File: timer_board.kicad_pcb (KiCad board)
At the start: 2 copper layers, 127 x 76.2 mm, 53 parts, among them IC1 ATMEGA32U4, K1 T9AS5D22-5, P1 USBMICRO, P2 OUT_INV, P3 Trigger, P4 OUT, Q1 NPN, Q2 NPN, U1 DS3231N, U2 74HC04, Y1 RESONATORSMD

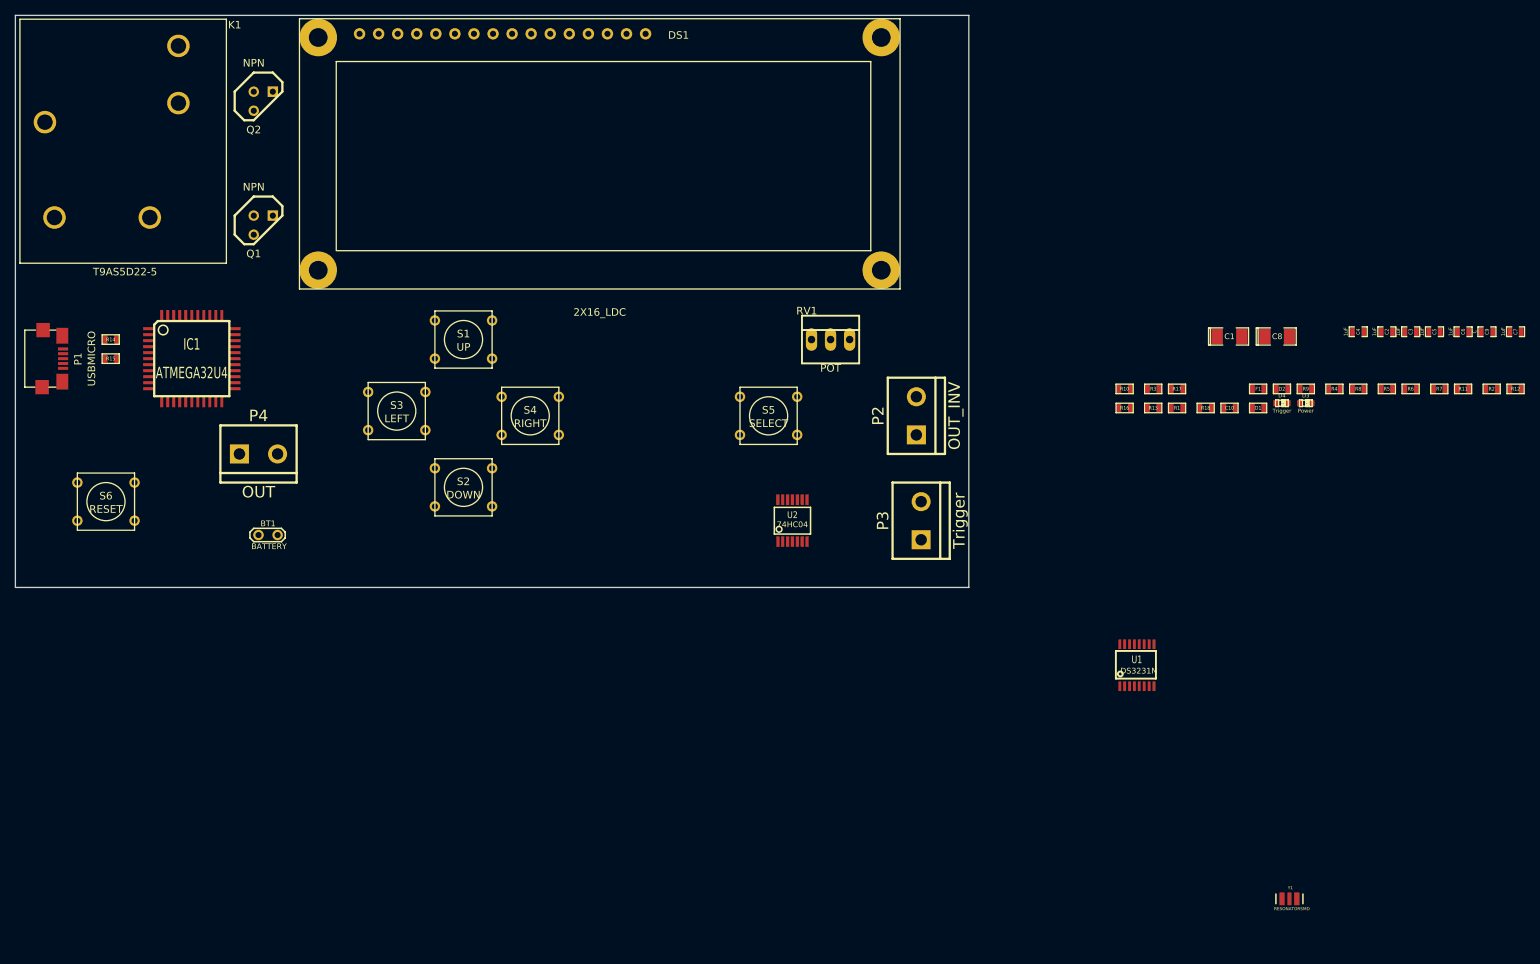
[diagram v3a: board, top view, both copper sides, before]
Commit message: Added battery holder
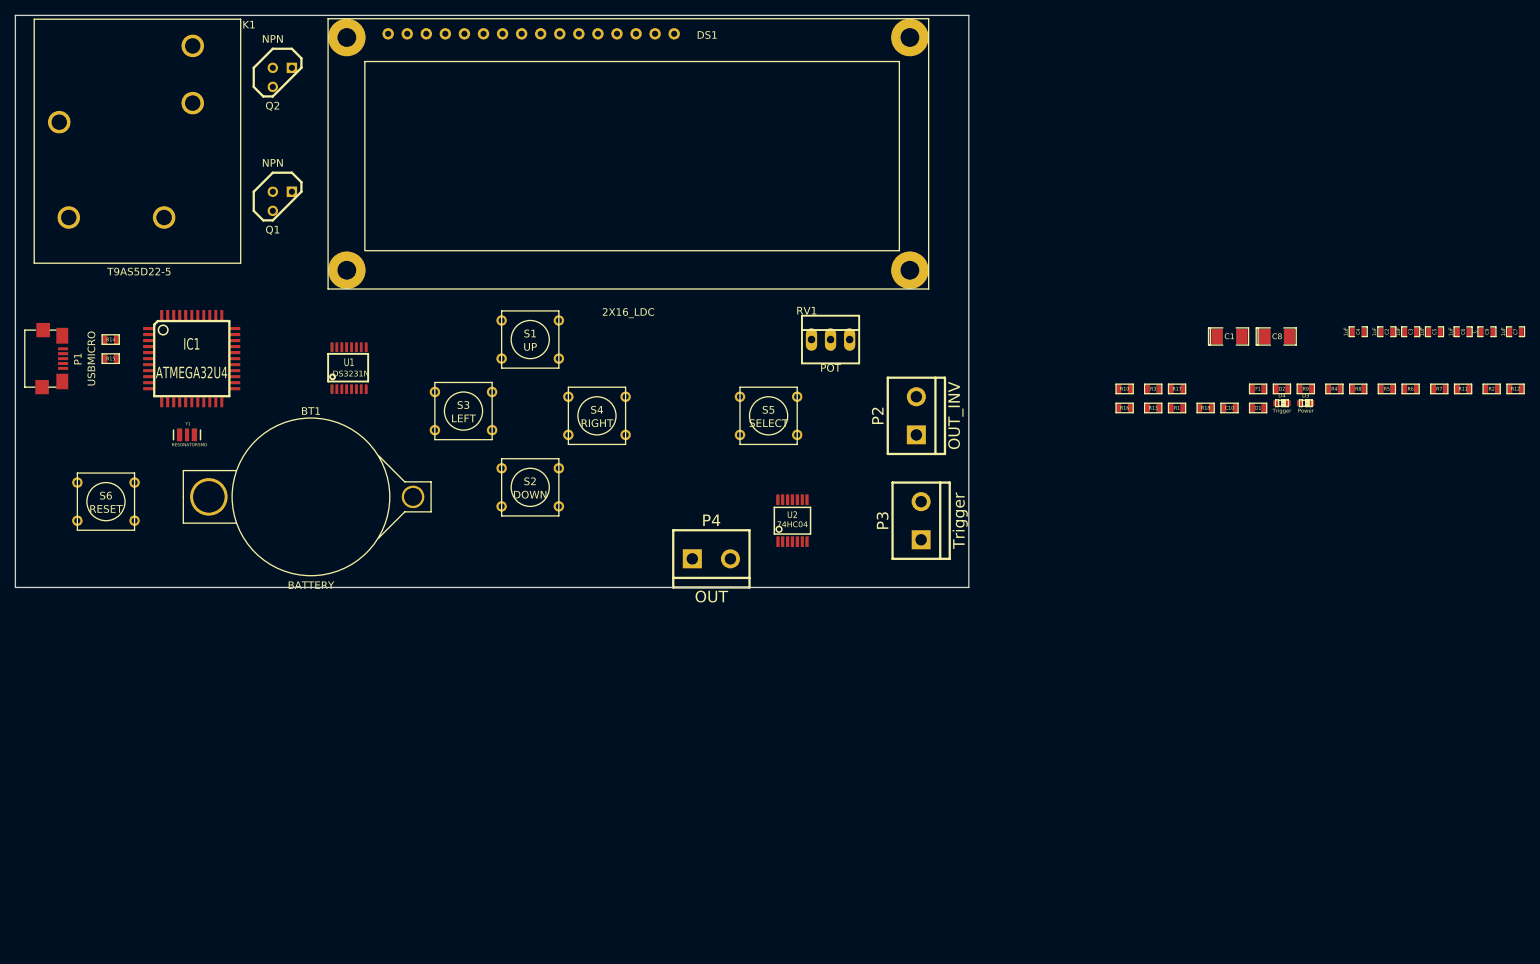
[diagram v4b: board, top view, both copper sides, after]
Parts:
- BT1: footprint TESTPOINT -> CR2032
- moved Y1 159.3 mm to (48.3, 81.3)
- moved U1 112.1 mm to (69.8, 72.4)
- moved P4 61.9 mm to (118.1, 97.8)
- moved S1 8.89 mm to (94.0, 68.6)
- moved S2 8.89 mm to (94.0, 88.3)
- moved S3 8.89 mm to (85.1, 78.1)
- moved S4 8.89 mm to (102.9, 78.7)
- moved BT1 7.65 mm to (64.8, 89.5)
- moved Q1 4.07 mm to (61.0, 50.2)
- moved Q2 4.07 mm to (61.0, 33.7)
- moved DS1 3.81 mm to (82.5, 29.8)
- moved K1 1.90 mm to (41.9, 41.9)
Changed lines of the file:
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@@
     (mod_text_width 0.15)
     (pad_size 3 3)
-    (pad_drill 2.06)
+    (pad_drill 2.4)
     (pad_to_mask_clearance 0)
     (aux_axis_origin 0 0)
@@
   )
   (module TSSOP16 (layer F.Cu)
-    (at 174.785 111.965)
+    (at 69.85 72.39)
     (attr smd)
     (fp_text reference U1 (at 0 -0.7493) (layer F.SilkS)
@@
   )
   (module TO92 (layer F.Cu)
-    (at 58.42 36.83)
+    (at 60.96 33.655)
     (descr "Transistor TO92 brochage type BC237")
     (tags "TR TO92")
@@
   )
   (module TO92 (layer F.Cu)
-    (at 58.42 53.34)
+    (at 60.96 50.165)
     (descr "Transistor TO92 brochage type BC237")
     (tags "TR TO92")
@@
     )
   )
-  (module TESTPOINT (layer F.Cu)
-    (at 59.055 94.615)
-    (descr "Connecteurs 2 pins")
-    (tags "CONN DEV")
-    (fp_text reference BT1 (at 0 -1.524) (layer F.SilkS)
-      (effects (font (size 0.762 0.762) (thickness 0.1524)))
-    )
-    (fp_text value BATTERY (at 0.127 1.524) (layer F.SilkS)
-      (effects (font (size 0.762 0.762) (thickness 0.1524)))
-    )
-    (fp_line (start -1.905 -0.889) (end 1.778 -0.889) (layer F.SilkS) (width 0.2032))
-    (fp_line (start 1.778 -0.889) (end 2.286 -0.381) (layer F.SilkS) (width 0.2032))
-    (fp_line (start 2.286 -0.381) (end 2.286 0.381) (layer F.SilkS) (width 0.2032))
-    (fp_line (start 2.286 0.381) (end 1.778 0.889) (layer F.SilkS) (width 0.2032))
-    (fp_line (start 1.778 0.889) (end -1.905 0.889) (layer F.SilkS) (width 0.2032))
-    (fp_line (start -1.905 0.889) (end -2.413 0.381) (layer F.SilkS) (width 0.2032))
-    (fp_line (start -2.413 0.381) (end -2.413 -0.381) (layer F.SilkS) (width 0.2032))
-    (fp_line (start -2.413 -0.381) (end -1.905 -0.889) (layer F.SilkS) (width 0.2032))
-    (pad 1 thru_hole circle (at -1.27 0) (size 1.397 1.397) (drill 0.8128)
-      (layers *.Cu *.Mask F.SilkS)
-      (net 31 N-000044)
-    )
-    (pad 1 thru_hole circle (at 1.27 0) (size 1.397 1.397) (drill 0.8128)
-      (layers *.Cu *.Mask F.SilkS)
-      (net 31 N-000044)
-    )
-    (model connectors/testpoint.wrl
-      (at (xyz 0 0 0))
-      (scale (xyz 1 1 1))
-      (rotate (xyz 0 0 0))
-    )
-  )
   (module SW_PUSH_SMALL (layer F.Cu)
     (at 37.465 90.17)
@@
   )
   (module SW_PUSH_SMALL (layer F.Cu)
-    (at 85.09 68.58)
+    (at 93.98 68.58)
     (fp_text reference S1 (at 0 -0.762) (layer F.SilkS)
       (effects (font (size 1.016 1.016) (thickness 0.2032)))
@@
   )
   (module SW_PUSH_SMALL (layer F.Cu)
-    (at 85.09 88.265)
+    (at 93.98 88.265)
     (fp_text reference S2 (at 0 -0.762) (layer F.SilkS)
       (effects (font (size 1.016 1.016) (thickness 0.2032)))
@@
   )
   (module SW_PUSH_SMALL (layer F.Cu)
-    (at 93.98 78.74)
+    (at 102.87 78.74)
     (fp_text reference S4 (at 0 -0.762) (layer F.SilkS)
       (effects (font (size 1.016 1.016) (thickness 0.2032)))
@@
   )
   (module SW_PUSH_SMALL (layer F.Cu)
-    (at 76.2 78.105)
+    (at 85.09 78.105)
     (fp_text reference S3 (at 0 -0.762) (layer F.SilkS)
       (effects (font (size 1.016 1.016) (thickness 0.2032)))
@@
   )
   (module bornier2 (layer F.Cu)
-    (at 57.785 83.82)
+    (at 118.11 97.79)
     (descr "Bornier d'alimentation 2 pins")
     (tags DEV)
@@
   )
   (module LCD16X2 (layer F.Cu)
-    (at 78.74 29.845)
+    (at 82.55 29.845)
     (fp_text reference DS1 (at 35 -1.8) (layer F.SilkS)
       (effects (font (size 1 1) (thickness 0.15)))
@@
   )
   (module T9AS5D22-5 (layer F.Cu)
-    (at 40.005 41.91)
+    (at 41.91 41.91)
     (fp_text reference K1 (at 14.605 -15.24) (layer F.SilkS)
       (effects (font (size 1 1) (thickness 0.15)))
@@
   )
   (module RESONATOR-SMD (layer F.Cu)
-    (at 195.105 143.08)
+    (at 48.26 81.28)
     (attr smd)
     (fp_text reference Y1 (at 0.127 -1.4732) (layer F.SilkS)
@@
     )
   )
+  (module CR2032 (layer F.Cu)
+    (at 64.77 89.535)
+    (fp_text reference BT1 (at 0 -11.4) (layer F.SilkS)
+      (effects (font (size 1 1) (thickness 0.15)))
+    )
+    (fp_text value BATTERY (at 0 11.8) (layer F.SilkS)
+      (effects (font (size 1 1) (thickness 0.15)))
+    )
+    (fp_line (start 12.5 2) (end 9 5.5) (layer F.SilkS) (width 0.15))
+    (fp_line (start 12.5 -2) (end 16 -2) (layer F.SilkS) (width 0.15))
+    (fp_line (start 16 -2) (end 16 2) (layer F.SilkS) (width 0.15))
+    (fp_line (start 16 2) (end 12.5 2) (layer F.SilkS) (width 0.15))
+    (fp_line (start 12.5 -2) (end 9 -5.5) (layer F.SilkS) (width 0.15))
+    (fp_line (start -17 0) (end -17 3.5) (layer F.SilkS) (width 0.15))
+    (fp_line (start -17 3.5) (end -10 3.5) (layer F.SilkS) (width 0.15))
+    (fp_line (start -17 0) (end -17 -3.5) (layer F.SilkS) (width 0.15))
+    (fp_line (start -17 -3.5) (end -10 -3.5) (layer F.SilkS) (width 0.15))
+    (fp_circle (center 0 0) (end 0.1 -10.5) (layer F.SilkS) (width 0.15))
+    (pad 1 thru_hole circle (at -13.6 0) (size 5 5) (drill 4.2)
+      (layers *.Cu *.Mask F.SilkS)
+      (net 31 N-000044)
+    )
+    (pad 2 thru_hole circle (at 13.6 0) (size 3 3) (drill 2.4)
+      (layers *.Cu *.Mask F.SilkS)
+      (net 9 GND)
+    )
+  )

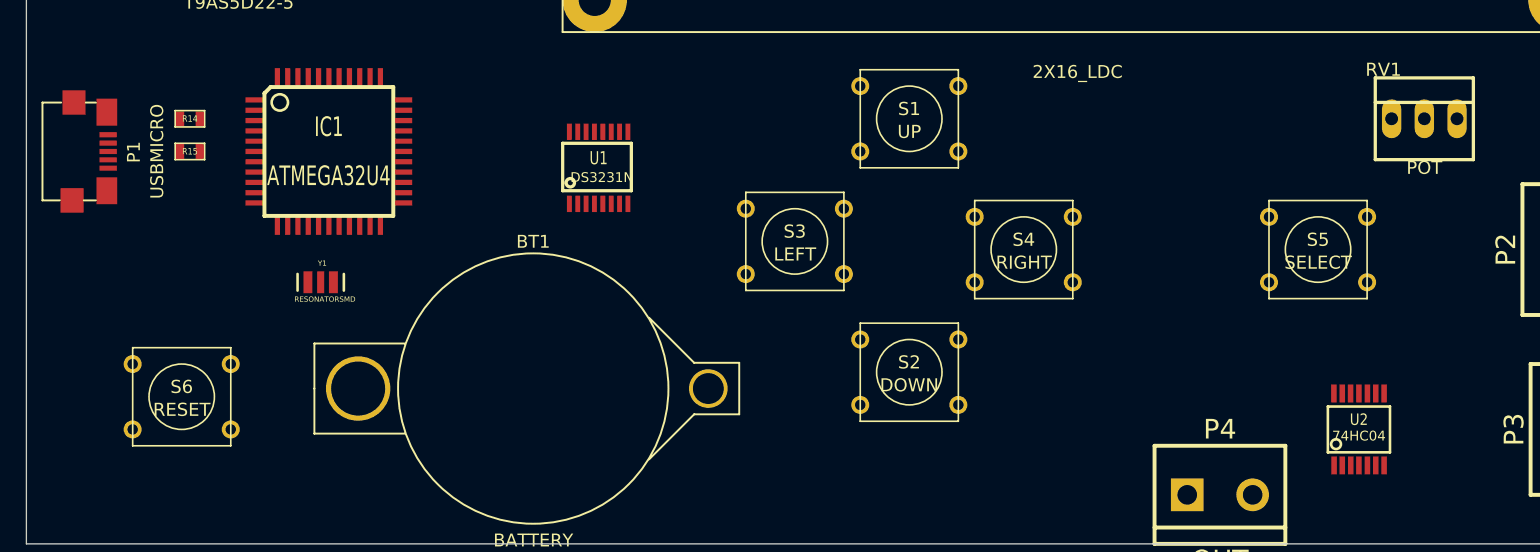
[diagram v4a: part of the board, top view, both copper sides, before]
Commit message: Added proper package for RTC and inverter
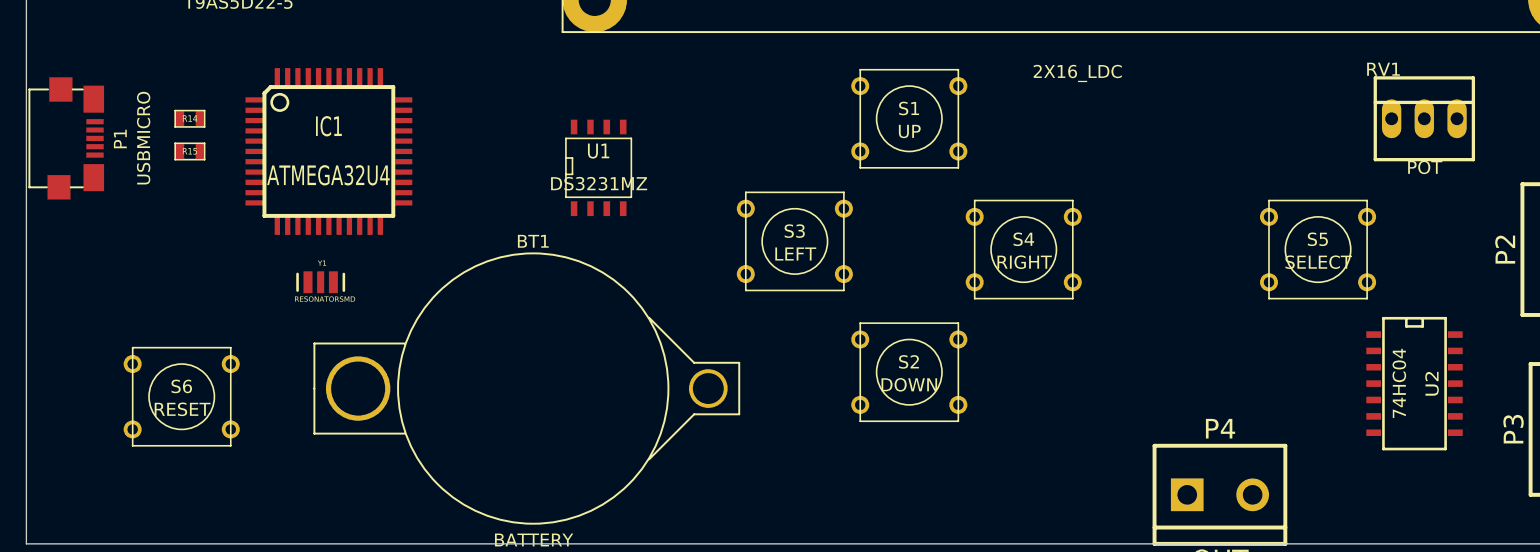
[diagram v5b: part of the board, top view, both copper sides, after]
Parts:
- U1: value DS3231N -> DS3231MZ; footprint TSSOP16 -> SO8N
- U2: footprint SSOP14 -> SO14N
- moved U2 5.69 mm to (133.3, 89.2), turned to 270 degrees
- moved P1 1.44 mm to (30.7, 70.1)
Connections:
- BT1 pad 1: N-000044 (its old number) -> N-000043
- U1 pad 5: N-000055 -> GND
- U1 pad 6: N-000055 -> N-000043
- U1 pad 7: N-000055 -> SDA
- U1 pad 8: N-000055 -> SCL
